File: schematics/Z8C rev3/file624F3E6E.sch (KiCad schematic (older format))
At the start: 7 parts

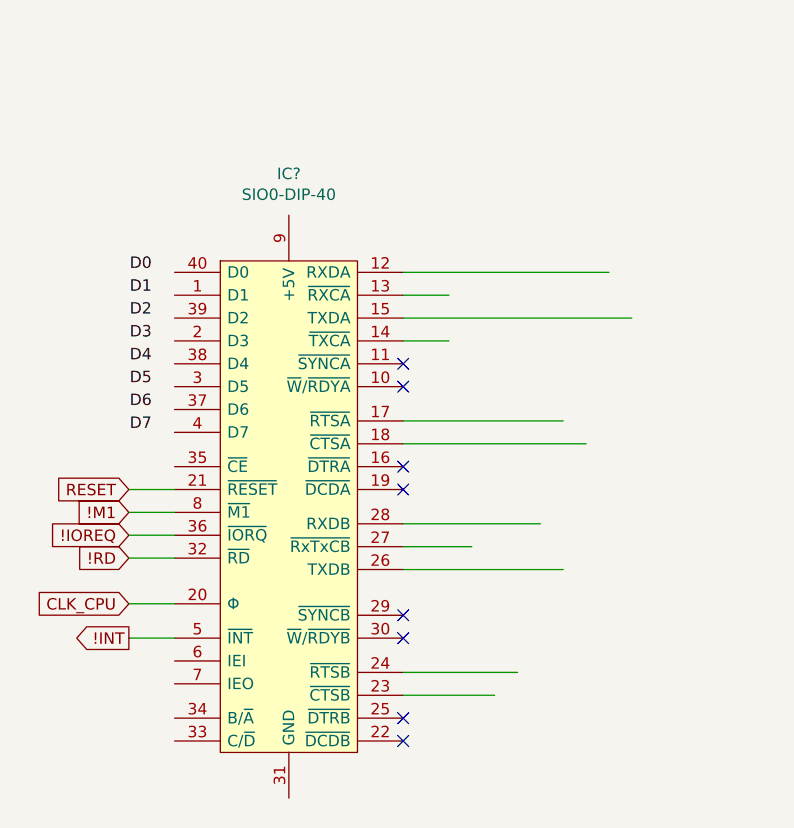
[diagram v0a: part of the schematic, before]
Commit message: working on sound
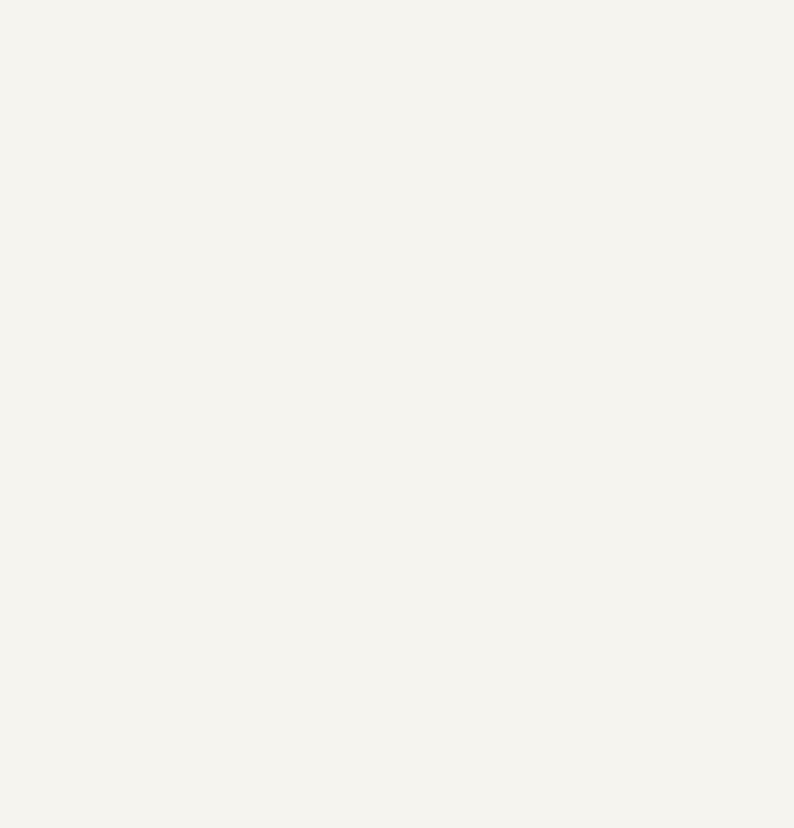
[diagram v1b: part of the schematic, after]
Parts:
- removed IC?: SIO0-DIP-40, Package_DIP:DIP-40_W15.24mm_LongPads, symbol Zilog_Z80_Peripherals:SIO0-DIP-40
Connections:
- net labels removed: D0, D1, D2, D3, D4, D5, D6, D7, RESET
- wire segments 125 -> 108
- no-connect marks 12 -> 4
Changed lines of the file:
@@
 $Descr A4 11693 8268
 encoding utf-8
-Sheet 6 6
+Sheet 6 7
 Title ""
 Date ""
@@
 Entry Wire Line
 	1900 1400 1800 1300
-Text Label -2500 2200 2    50   ~ 0
-D0
 Wire Wire Line
 	2500 1500 1900 1500
 Entry Wire Line
 	1900 1500 1800 1400
-Text Label -2500 2300 2    50   ~ 0
-D1
 Wire Wire Line
 	2500 1600 1900 1600
 Entry Wire Line
 	1900 1600 1800 1500
-Text Label -2500 2400 2    50   ~ 0
-D2
 Wire Wire Line
 	2500 1700 1900 1700
 Entry Wire Line
 	1900 1700 1800 1600
-Text Label -2500 2500 2    50   ~ 0
-D3
 Wire Wire Line
 	2500 1800 1900 1800
 Entry Wire Line
 	1900 1800 1800 1700
-Text Label -2500 2600 2    50   ~ 0
-D4
 Wire Wire Line
 	2500 1900 1900 1900
 Entry Wire Line
 	1900 1900 1800 1800
-Text Label -2500 2700 2    50   ~ 0
-D5
 Wire Wire Line
 	2500 2000 1900 2000
 Entry Wire Line
 	1900 2000 1800 1900
-Text Label -2500 2800 2    50   ~ 0
-D6
 Wire Wire Line
 	2500 2100 1900 2100
 Entry Wire Line
 	1900 2100 1800 2000
-Text Label -2500 2900 2    50   ~ 0
-D7
 Wire Wire Line
 	2500 2400 1900 2400
@@
 Text Label 2400 2300 2    50   ~ 0
 A1
-Text GLabel -2600 3250 0    50   Input ~ 0
-!M1
-Text GLabel -2600 3350 0    50   Input ~ 0
-!IOREQ
-Text GLabel -2600 3450 0    50   Input ~ 0
-!RD
-Wire Wire Line
-	-2600 3250 -2400 3250
-Wire Wire Line
-	-2400 3350 -2600 3350
-Wire Wire Line
-	-2600 3450 -2400 3450
-Text GLabel -2600 3150 0    50   Input ~ 0
-RESET
-Wire Wire Line
-	-2600 3150 -2400 3150
-Text GLabel -2600 3650 0    50   Input ~ 0
-CLK_CPU
-Wire Wire Line
-	-2400 3650 -2600 3650
-Text GLabel -2600 3800 0    50   Output ~ 0
-!INT
-Wire Wire Line
-	-2400 3800 -2600 3800
-Wire Wire Line
-	-1400 2500 -1200 2500
-Wire Wire Line
-	-1200 2300 -1400 2300
-Wire Wire Line
-	-1400 3400 -1100 3400
-Wire Wire Line
-	-1400 2400 -400 2400
-Wire Wire Line
-	-1400 2200 -500 2200
-Wire Wire Line
-	-1400 2850 -700 2850
-Wire Wire Line
-	-1400 2950 -600 2950
-Wire Wire Line
-	-700 3500 -1400 3500
-Wire Wire Line
-	-800 3300 -1400 3300
-Wire Wire Line
-	-900 3950 -1400 3950
-Wire Wire Line
-	-1000 4050 -1400 4050
 Wire Bus Line
 	1800 950  1000 950
-NoConn ~ -1400 2600
-NoConn ~ -1400 2700
-NoConn ~ -1400 3050
-NoConn ~ -1400 3150
-NoConn ~ -1400 3700
-NoConn ~ -1400 4150
-NoConn ~ -1400 4250
-NoConn ~ -1400 3800
-$Comp
-L Zilog_Z80_Peripherals:SIO0-DIP-40 IC?
-U 1 1 624FB9ED
-P -2200 2150
-AR Path="/622409DC/624FB9ED" Ref="IC?"  Part="1"
-AR Path="/624F3E6F/624FB9ED" Ref="IC?"  Part="1"
-F 0 "IC?" H -1900 2531 50  0000 C CNN
-F 1 "SIO0-DIP-40" H -1900 2440 50  0000 C CNN
-F 2 "Package_DIP:DIP-40_W15.24mm_LongPads" H -1800 4000 50  0001 L CNN
-F 3 "" H -3000 1000 50  0001 L CNN
-F 4 "Z80 CMOS SIO/0 Z84C40 Zilog" H -1800 3800 50  0001 L CNN "Description"
-F 5 "4.06" H -1800 3700 50  0001 L CNN "Height"
-F 6 "Zilog" H -1800 3600 50  0001 L CNN "Manufacturer_Name"
-F 7 "Z84C4206PEG" H -1800 3500 50  0001 L CNN "Manufacturer_Part_Number"
-F 8 "692-Z84C4206PEG" H -1800 3400 50  0001 L CNN "Mouser Part Number"
-F 9 "https://www.mouser.com/Search/Refine.aspx?Keyword=692-Z84C4206PEG" H -1800 3300 50  0001 L CNN "Mouser Price/Stock"
-F 10 "6600766" H -1800 3200 50  0001 L CNN "RS Part Number"
-F 11 "https://uk.rs-online.com/web/p/products/6600766" H -1800 3100 50  0001 L CNN "RS Price/Stock"
-F 12 "R1000052" H -1800 3000 50  0001 L CNN "Allied_Number"
-F 13 "https://www.alliedelec.com/zilog-z84c4206peg/R1000052/" H -1800 2900 50  0001 L CNN "Allied Price/Stock"
-	1    -2200 2150
-	1    0    0    -1
-$EndComp
 $Comp
 L Zilog_Z80_Peripherals:PIO-DIP-40 U?
@@
 Wire Wire Line
 	8400 2750 8400 2400
-Wire Bus Line
-	1800 950  1800 2300
 Connection ~ 8400 2400
 Text Label 10300 1700 2    50   ~ 0
@@
 	1    0    0    -1
 $EndComp
+Wire Bus Line
+	1800 950  1800 2300
 $EndSCHEMATC

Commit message: added bank switching, apu, dma and IRQ logic. Misc. improvements
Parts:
- U?: symbol Zilog_Z80_Peripherals:PIO-DIP-40 -> Z8C-rev3-rescue:PIO-DIP-40-Zilog_Z80_Peripherals
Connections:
- net IO_PS2_CS: now reaches U?.4 (~CE~)
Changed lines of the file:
@@
 	1800 950  1000 950
 $Comp
-L Zilog_Z80_Peripherals:PIO-DIP-40 U?
+L Z8C-rev3-rescue:PIO-DIP-40-Zilog_Z80_Peripherals U?
 U 1 1 624FCE64
 P 2600 1300
@@
 	1    0    0    -1
 $EndComp
+Text GLabel 2300 2600 0    50   Input ~ 0
+IO_PS2_CS
+Wire Wire Line
+	2300 2600 2500 2600
 Wire Bus Line
 	1800 950  1800 2300
